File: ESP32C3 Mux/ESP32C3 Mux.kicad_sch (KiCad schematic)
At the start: 4 parts

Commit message: finished esp32 mux schematic
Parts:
- added J1: 6130XX243121_613020243121, ESP32C3 Mux:613020243121, symbol ESP32C3Mux:6130XX243121_613020243121
- added JP? (x2): Jumper_2_Small_Open, symbol Jumper:Jumper_2_Small_Open
- added R? (x2): 10k, symbol Device:R
- gave numbers to parts that had none: 4
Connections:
- net +3V3: now also J1.1, J1.13, J1.17, J1.5, J1.9, R?.1, R?.1
- net GND: now also U1.13 (GND), U2.1 (A0), U2.2 (A1), U2.21 (A2), J1.12, J1.16, J1.20, J1.4, J1.8
- net SDA3: now reaches U2.10 (SD3)
- net SDA3: now also J1.15
- net SCL3: now reaches U2.11 (SC3)
- net SCL3: now also J1.14
- net SDA4: now reaches U2.13 (SD4)
- net SDA4: now also J1.19
- net SCL4: now reaches U2.14 (SC4)
- net SCL4: now also J1.18
- net SCL: now reaches U2.22 (SCL)
- net SCL: now also U1.1 (D0), JP?.1 (A)
- net SDA: now reaches U2.23 (SDA)
- net SDA: now also U1.2 (D1), JP?.1 (A)
- net SDA0: now reaches U2.4 (SD0)
- net SDA0: now also J1.3
- net SCL0: now reaches U2.5 (SC0)
- net SCL0: now also J1.2
- net SDA1: now reaches U2.6 (SD1)
- net SDA1: now also J1.7
- net SCL1: now reaches U2.7 (SC1)
- net SCL1: now also J1.6
- net SDA2: now reaches U2.8 (SD2)
- net SDA2: now also J1.11
- net SCL2: now reaches U2.9 (SC2)
- net SCL2: now also J1.10
- new net: JP?.2 (B), R?.2 (x2)
- no-connect marks 10 -> 16
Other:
- moved on the sheet: R1, U1, U2

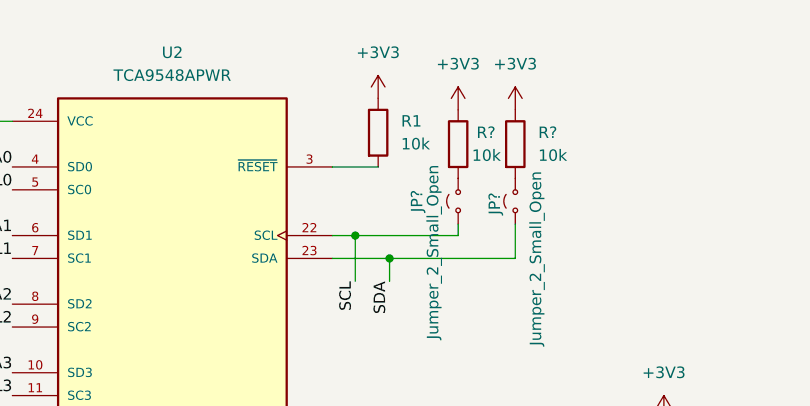
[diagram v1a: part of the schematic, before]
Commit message: fixed power flag errors
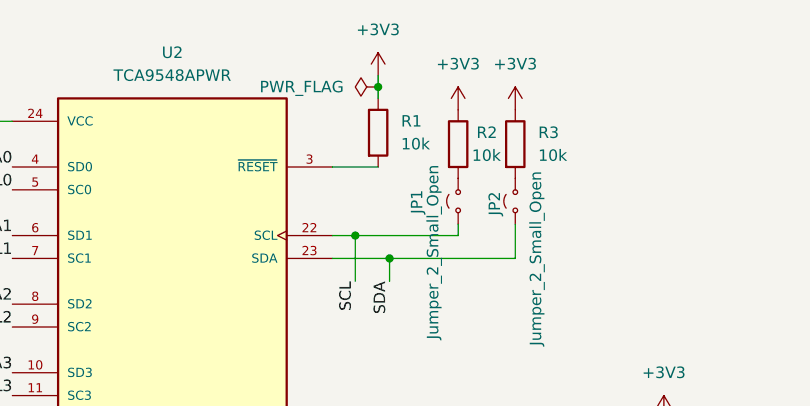
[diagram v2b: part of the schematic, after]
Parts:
- U1: footprint 113991054:MODULE_113991054 -> ESP32C3 Mux:ESP32C3
- U2: footprint TCA9548APWR:SOP65P640X120-24N -> ESP32C3 Mux:TCA9548APWR
- gave numbers to parts that had none: 4
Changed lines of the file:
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@@
+	)
+	(junction
+		(at 200.66 55.88)
+		(diameter 0)
+		(color 0 0 0 0)
 	)
 	(junction
@@
 	(wire
 		(pts
+			(xy 200.66 55.88) (xy 200.66 57.15)
+		)
+		(stroke
+			(width 0)
+			(type default)
+		)
+	)
+	(wire
+		(pts
 			(xy 86.36 113.03) (xy 87.63 113.03)
 		)
@@
 		(pts
 			(xy 232.41 92.71) (xy 232.41 95.25)
+		)
+		(stroke
+			(width 0)
+			(type default)
+		)
+	)
+	(wire
+		(pts
+			(xy 200.66 54.61) (xy 200.66 55.88)
 		)
 		(stroke
@@
 		(on_board yes)
 		(dnp no)
-		(property "Reference" "JP?"
+		(property "Reference" "JP1"
 			(at 204.978 67.31 0)
 			(effects
@@
 			(project ""
 				(path "/e2712e9e-3de3-412e-81b5-ba5ff5ca700b"
-					(reference "JP?")
+					(reference "JP1")
 					(unit 1)
 				)
@@
 		(dnp no)
 		(fields_autoplaced yes)
-		(property "Reference" "R?"
+		(property "Reference" "R3"
 			(at 218.44 60.9599 0)
 			(effects
@@
 			(project "ESP32C3 Mux"
 				(path "/e2712e9e-3de3-412e-81b5-ba5ff5ca700b"
-					(reference "R?")
+					(reference "R3")
 					(unit 1)
 				)
@@
 			)
 		)
-		(property "Footprint" "TCA9548APWR:SOP65P640X120-24N"
+		(property "Footprint" "ESP32C3 Mux:TCA9548APWR"
 			(at 177.8 92.71 0)
 			(effects
@@
 	(symbol
 		(lib_id "power:+3V3")
-		(at 200.66 57.15 0)
+		(at 200.66 54.61 0)
 		(unit 1)
 		(exclude_from_sim no)
@@
 		(fields_autoplaced yes)
 		(property "Reference" "#PWR01"
-			(at 200.66 60.96 0)
+			(at 200.66 58.42 0)
 			(effects
 				(font
@@
 		)
 		(property "Value" "+3V3"
-			(at 200.66 52.07 0)
+			(at 200.66 49.53 0)
 			(effects
 				(font
@@
 		)
 		(property "Footprint" ""
-			(at 200.66 57.15 0)
+			(at 200.66 54.61 0)
 			(effects
 				(font
@@
 		)
 		(property "Datasheet" ""
-			(at 200.66 57.15 0)
+			(at 200.66 54.61 0)
 			(effects
 				(font
@@
 		)
 		(property "Description" "Power symbol creates a global label with name \"+3V3\""
-			(at 200.66 57.15 0)
+			(at 200.66 54.61 0)
 			(effects
 				(font
@@
 		(on_board yes)
 		(dnp no)
-		(property "Reference" "JP?"
+		(property "Reference" "JP2"
 			(at 213.614 68.834 0)
 			(effects
@@
 			(project ""
 				(path "/e2712e9e-3de3-412e-81b5-ba5ff5ca700b"
-					(reference "JP?")
+					(reference "JP2")
 					(unit 1)
 				)
@@
 			)
 		)
-		(property "Footprint" "113991054:MODULE_113991054"
+		(property "Footprint" "ESP32C3 Mux:ESP32C3"
 			(at 254 107.95 0)
 			(effects
@@
 	)
 	(symbol
+		(lib_id "power:PWR_FLAG")
+		(at 200.66 55.88 90)
+		(unit 1)
+		(exclude_from_sim no)
+		(in_bom yes)
+		(on_board yes)
+		(dnp no)
+		(fields_autoplaced yes)
+		(property "Reference" "#FLG01"
+			(at 198.755 55.88 0)
+			(effects
+				(font
+					(size 1.27 1.27)
+				)
+				(hide yes)
+			)
+		)
+		(property "Value" "PWR_FLAG"
+			(at 196.85 55.8799 90)
+			(effects
+				(font
+					(size 1.27 1.27)
+				)
+				(justify left)
+			)
+		)
+		(property "Footprint" ""
+			(at 200.66 55.88 0)
+			(effects
+				(font
+					(size 1.27 1.27)
+				)
+				(hide yes)
+			)
+		)
+		(property "Datasheet" "~"
+			(at 200.66 55.88 0)
+			(effects
+				(font
+					(size 1.27 1.27)
+				)
+				(hide yes)
+			)
+		)
+		(property "Description" "Special symbol for telling ERC where power comes from"
+			(at 200.66 55.88 0)
+			(effects
+				(font
+					(size 1.27 1.27)
+				)
+				(hide yes)
+			)
+		)
+		(pin "1"
+		)
+		(instances
+			(project ""
+				(path "/e2712e9e-3de3-412e-81b5-ba5ff5ca700b"
+					(reference "#FLG01")
+					(unit 1)
+				)
+			)
+		)
+	)
+	(symbol
 		(lib_id "power:+3V3")
 		(at 148.59 57.15 0)
@@
 		(on_board yes)
 		(dnp no)
-		(property "Reference" "R?"
+		(property "Reference" "R2"
 			(at 211.582 60.96 0)
 			(effects
@@
 			(project "ESP32C3 Mux"
 				(path "/e2712e9e-3de3-412e-81b5-ba5ff5ca700b"
-					(reference "R?")
+					(reference "R2")
 					(unit 1)
 				)

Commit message: forgot to save kicad file lol
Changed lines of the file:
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@@
+	)
+	(junction
+		(at 148.59 127)
+		(diameter 0)
+		(color 0 0 0 0)
 	)
 	(junction
@@
 	(wire
 		(pts
+			(xy 148.59 127) (xy 148.59 128.27)
+		)
+		(stroke
+			(width 0)
+			(type default)
+		)
+	)
+	(wire
+		(pts
 			(xy 198.12 72.39) (xy 209.55 72.39)
 		)
@@
 	(wire
 		(pts
-			(xy 148.59 125.73) (xy 148.59 128.27)
+			(xy 148.59 125.73) (xy 148.59 127)
 		)
 		(stroke
@@
 					(unit 1)
 				)
+			)
+		)
+	)
+	(symbol
+		(lib_id "power:PWR_FLAG")
+		(at 148.59 127 90)
+		(unit 1)
+		(exclude_from_sim no)
+		(in_bom yes)
+		(on_board yes)
+		(dnp no)
+		(fields_autoplaced yes)
+		(property "Reference" "#FLG02"
+			(at 146.685 127 0)
+			(effects
+				(font
+					(size 1.27 1.27)
+				)
+				(hide yes)
+			)
+		)
+		(property "Value" "PWR_FLAG"
+			(at 144.78 126.9999 90)
+			(effects
+				(font
+					(size 1.27 1.27)
+				)
+				(justify left)
+			)
+		)
+		(property "Footprint" ""
+			(at 148.59 127 0)
+			(effects
+				(font
+					(size 1.27 1.27)
+				)
+				(hide yes)
+			)
+		)
+		(property "Datasheet" "~"
+			(at 148.59 127 0)
+			(effects
+				(font
+					(size 1.27 1.27)
+				)
+				(hide yes)
+			)
+		)
+		(property "Description" "Special symbol for telling ERC where power comes from"
+			(at 148.59 127 0)
+			(effects
+				(font
+					(size 1.27 1.27)
+				)
+				(hide yes)
+			)
+		)
+		(pin "1"
+		)
+		(instances
+			(project ""
+				(path "/e2712e9e-3de3-412e-81b5-ba5ff5ca700b"
+					(reference "#FLG02")
+					(unit 1)
+				)

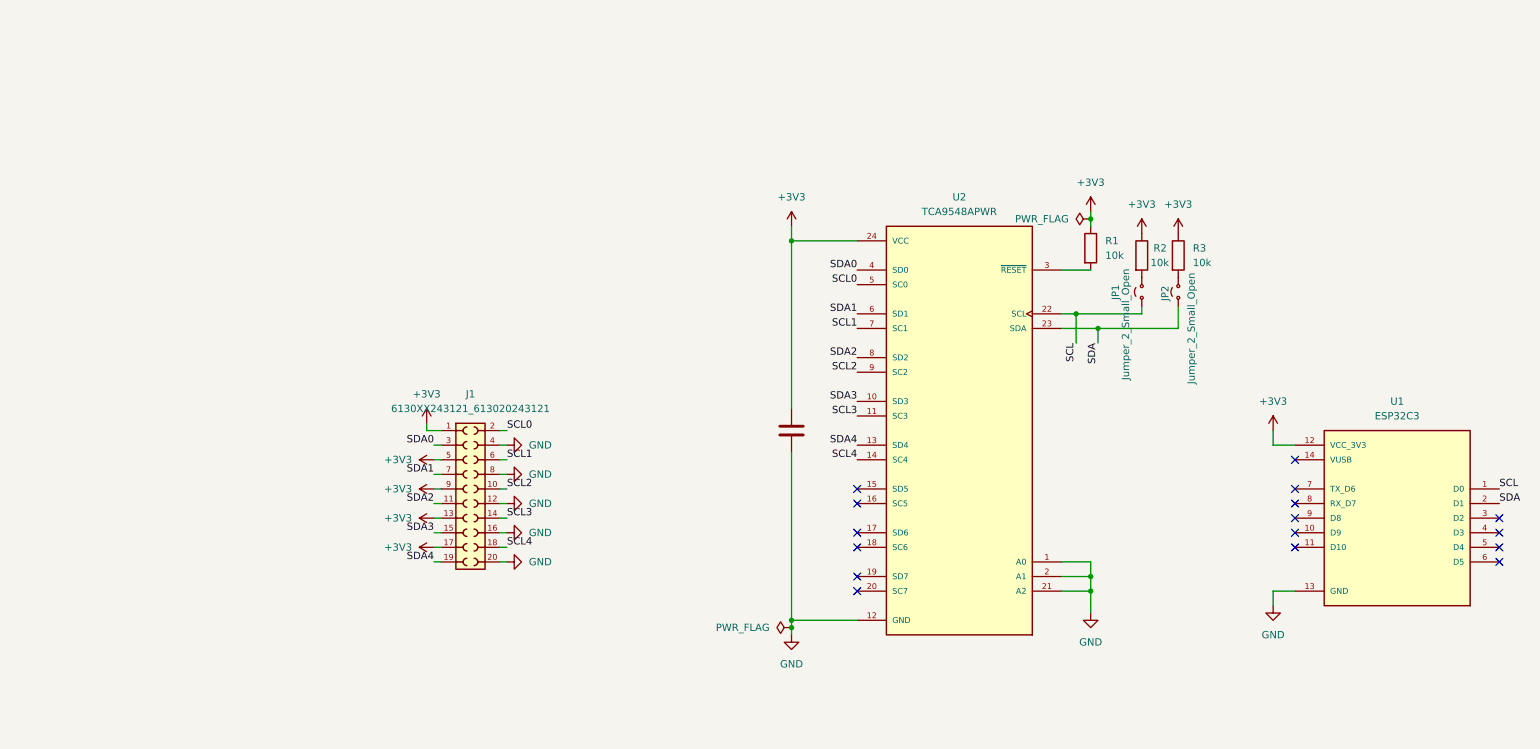
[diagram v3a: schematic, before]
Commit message: start layout for sensor control
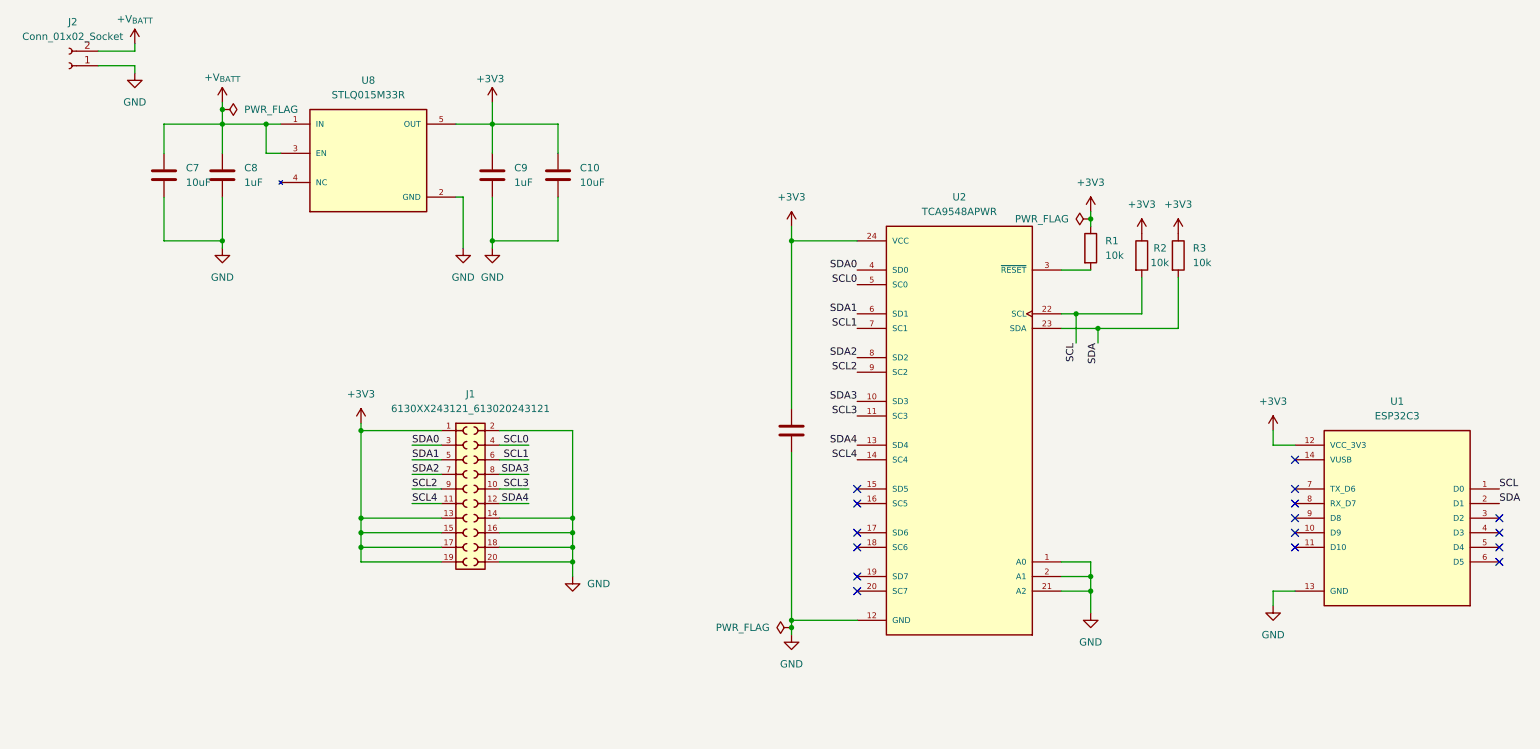
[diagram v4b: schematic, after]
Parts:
- removed JP1, JP2: Jumper_2_Small_Open, symbol Jumper:Jumper_2_Small_Open
- added C10, C7: 10uF, Capacitor_SMD:C_0805_2012Metric, symbol Device:C
- added C8, C9: 1uF, Capacitor_SMD:C_0805_2012Metric, symbol Device:C
- added J2: Conn_01x02_Socket, Connector_JST:JST_PH_B2B-PH-K_1x02_P2.00mm_Vertical, symbol Connector:Conn_01x02_Socket
- added U8: STLQ015M33R, ESP32C3 Mux:SOT95P280X145-5N, symbol STLQ015M33R:STLQ015M33R
- C1: footprint (none) -> Capacitor_SMD:C_0805_2012Metric
- R1, R2, R3: footprint (none) -> Resistor_SMD:R_0805_2012Metric_Pad1.20x1.40mm_HandSolder
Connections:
- net +3V3: now also J1.15, J1.19, C10.1, C9.1, U8.5 (OUT); no longer J1.5, J1.9
- net GND: now also J1.14, J1.18, J1.2, C10.2, C7.2, C8.2, C9.2, J2.1 (Pin_1), U8.2 (GND); no longer J1.12, J1.4, J1.8
- net SCL: now also R2.2
- net SCL0: now also J1.4; no longer J1.2
- net SCL2: now also J1.9; no longer J1.10
- net SCL3: now also J1.10; no longer J1.14
- net SCL4: now also J1.11; no longer J1.18
- net SDA: now also R3.2
- net SDA1: now also J1.5; no longer J1.7
- net SDA2: now also J1.7; no longer J1.11
- net SDA3: now also J1.8; no longer J1.15
- net SDA4: now also J1.12; no longer J1.19
- new net +V_{BATT}: C7.1, C8.1, J2.2 (Pin_2), U8.1 (IN), U8.3 (EN)

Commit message: finished layout
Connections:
- net SCL2: now also J1.8; no longer J1.9
- net SDA3: now also J1.9; no longer J1.8
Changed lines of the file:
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@@
+		)
+	)
+	(label "SDA3"
+		(at 82.55 102.87 0)
+		(effects
+			(font
+				(size 1.27 1.27)
+			)
+			(justify left bottom)
 		)
 	)
@@
 		)
 	)
-	(label "SDA3"
-		(at 102.87 100.33 180)
-		(effects
-			(font
-				(size 1.27 1.27)
-			)
-			(justify right bottom)
-		)
-	)
 	(label "SCL"
 		(at 198.12 77.47 270)
@@
 			)
 			(justify right bottom)
-		)
-	)
-	(label "SCL2"
-		(at 82.55 102.87 0)
-		(effects
-			(font
-				(size 1.27 1.27)
-			)
-			(justify left bottom)
 		)
 	)
@@
 		)
 	)
+	(label "SCL0"
+		(at 102.87 95.25 180)
+		(effects
+			(font
+				(size 1.27 1.27)
+			)
+			(justify right bottom)
+		)
+	)
+	(label "SDA0"
+		(at 82.55 95.25 0)
+		(effects
+			(font
+				(size 1.27 1.27)
+			)
+			(justify left bottom)
+		)
+	)
 	(label "SCL2"
 		(at 160.02 82.55 180)
@@
 		)
 	)
-	(label "SDA0"
-		(at 82.55 95.25 0)
-		(effects
-			(font
-				(size 1.27 1.27)
-			)
-			(justify left bottom)
-		)
-	)
 	(label "SDA"
 		(at 271.78 105.41 0)
@@
 		)
 	)
-	(label "SCL0"
-		(at 102.87 95.25 180)
+	(label "SCL2"
+		(at 102.87 100.33 180)
 		(effects
 			(font

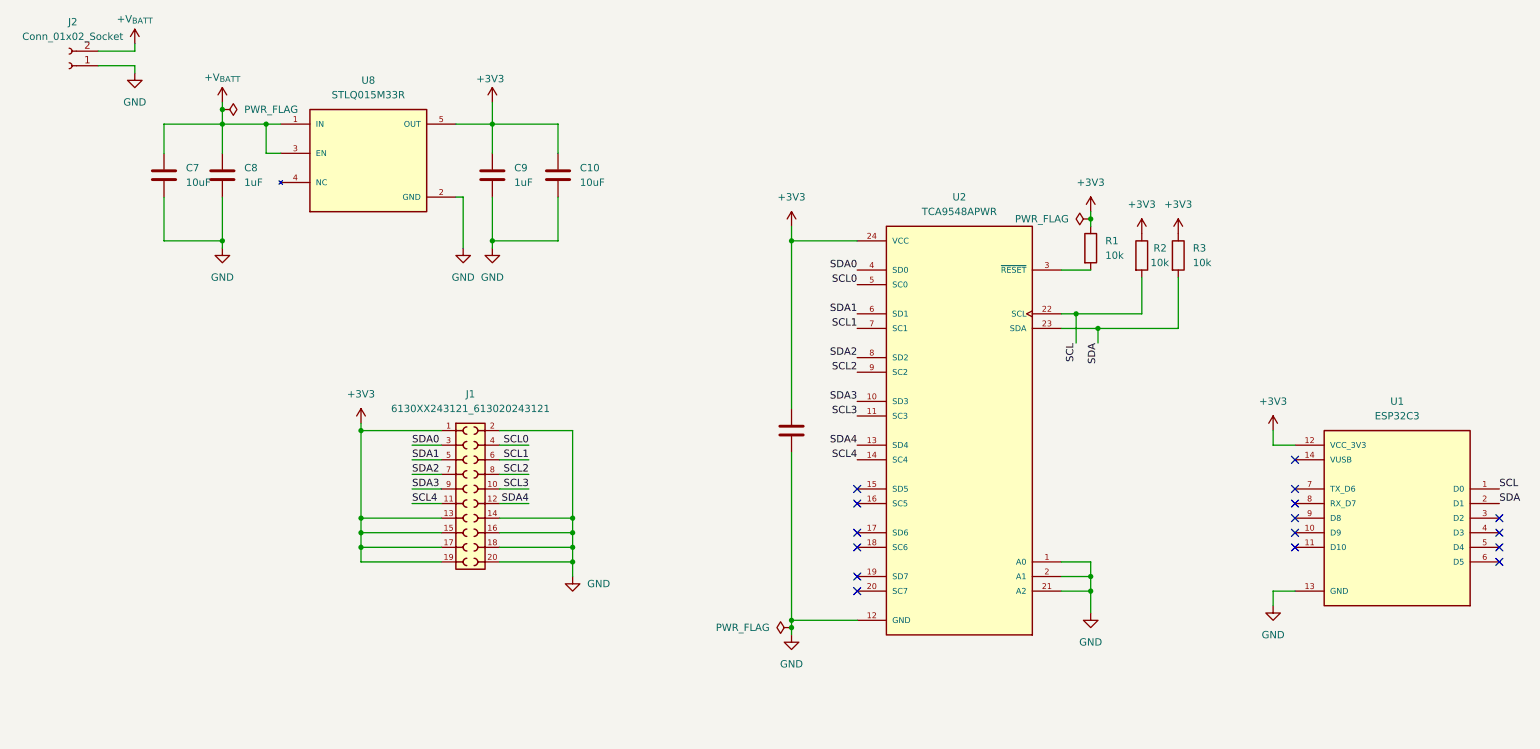
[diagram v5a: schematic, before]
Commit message: removed mux and added 2 2x8 pin headers
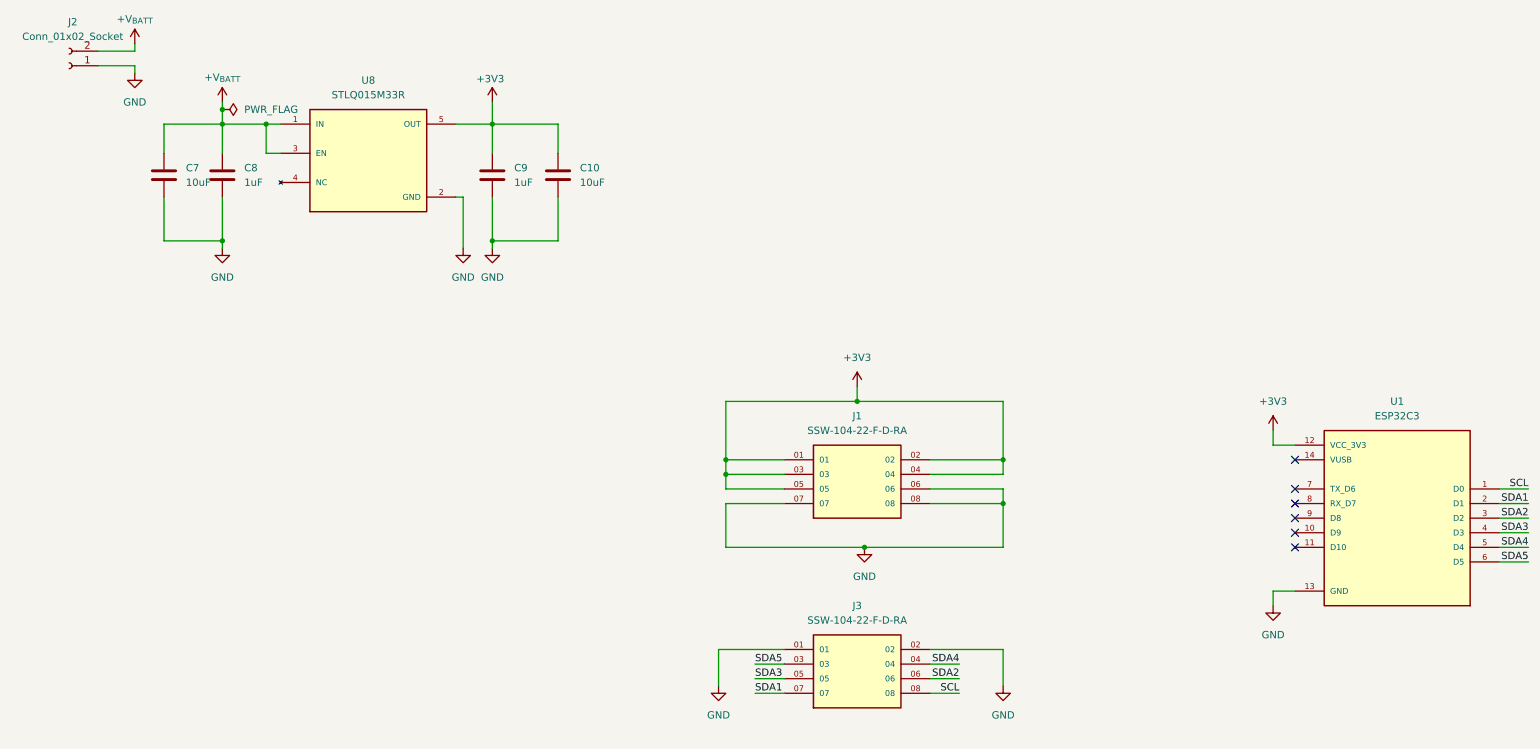
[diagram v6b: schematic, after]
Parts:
- removed C1: 10uF, Capacitor_SMD:C_0805_2012Metric, symbol Device:C
- removed J1: 6130XX243121_613020243121, ESP32C3 Mux:613020243121, symbol ESP32C3Mux:6130XX243121_613020243121
- removed R1, R2, R3: 10k, Resistor_SMD:R_0805_2012Metric_Pad1.20x1.40mm_HandSolder, symbol Device:R
- removed U2: TCA9548APWR, ESP32C3 Mux:TCA9548APWR, symbol ESP32C3Mux:TCA9548APWR
- added J1, J3: SSW-104-22-F-D-RA, ESP32C3 Mux:SAMTEC_SSW-104-22-F-D-RA, symbol ESP32C3Mux:SSW-104-22-F-D-RA
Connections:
- net SDA is gone; now on net SDA1: U1.2 (D1)
- net +3V3: now also J1.01, J1.02, J1.03, J1.04, J1.05
- net GND: now also J1.06, J1.07, J1.08, J3.01, J3.02
- net SCL: now also J3.08
- net SDA1: now also J3.07
- net SDA2: now also U1.3 (D2), J3.06
- net SDA3: now also U1.4 (D3), J3.05
- net SDA4: now also U1.5 (D4), J3.04
- net SDA5: now reaches U1.6 (D5)
- net SDA5: now also J3.03
- no-connect marks 16 -> 6

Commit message: updates
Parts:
- removed J1, J3: SSW-104-22-F-D-RA, ESP32C3 Mux:SAMTEC_SSW-104-22-F-D-RA, symbol ESP32C3Mux:SSW-104-22-F-D-RA
- added J1: 6130XX243121_613020243121, ESP32C3 Mux:613020243121, symbol ESP32C3Mux:6130XX243121_613020243121
- C10, C7, C8, C9: footprint Capacitor_SMD:C_0805_2012Metric -> Capacitor_SMD:C_0805_2012Metric_Pad1.18x1.45mm_HandSolder
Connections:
- net SDA5 is gone; now on net SDA4: U1.6 (D5)
- net +3V3: now also J1.11, J1.13, J1.15, J1.17, J1.19
- net GND: now also J1.14, J1.16, J1.18, J1.2, J1.20
- net SCL: now also J1.1, J1.3, J1.5, J1.7, J1.9
- net SDA1: now also U1.3 (D2), J1.6; no longer U1.2 (D1)
- net SDA2: now also U1.4 (D3), J1.8; no longer U1.3 (D2)
- net SDA3: now also U1.5 (D4), J1.10; no longer U1.4 (D3)
- net SDA4: now also J1.12; no longer U1.5 (D4)
- new net SDA0: J1.4, U1.2 (D1)
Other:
- moved on the sheet: C10, C7, C8, C9, J2, U1, U8
